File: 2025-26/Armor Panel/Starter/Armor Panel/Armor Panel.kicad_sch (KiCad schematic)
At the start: 10 parts

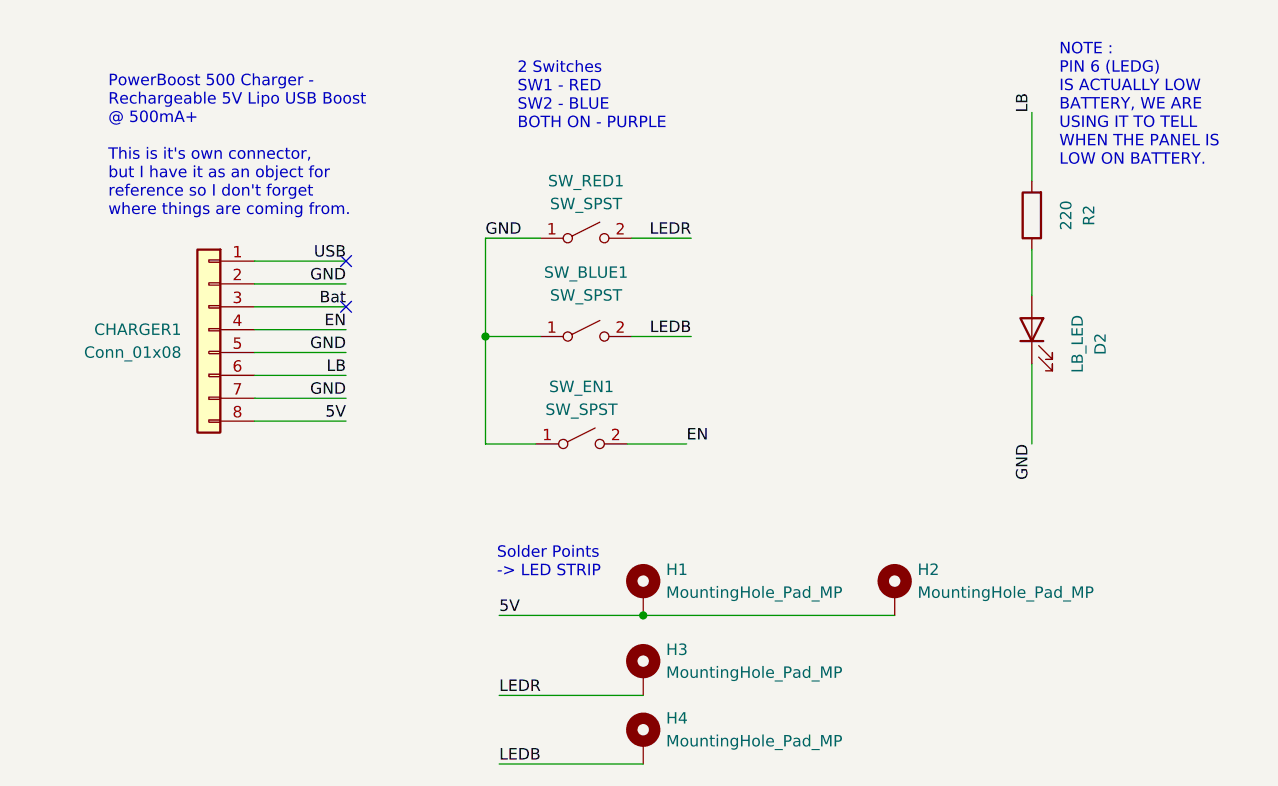
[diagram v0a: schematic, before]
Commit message: Forgot to connect pads
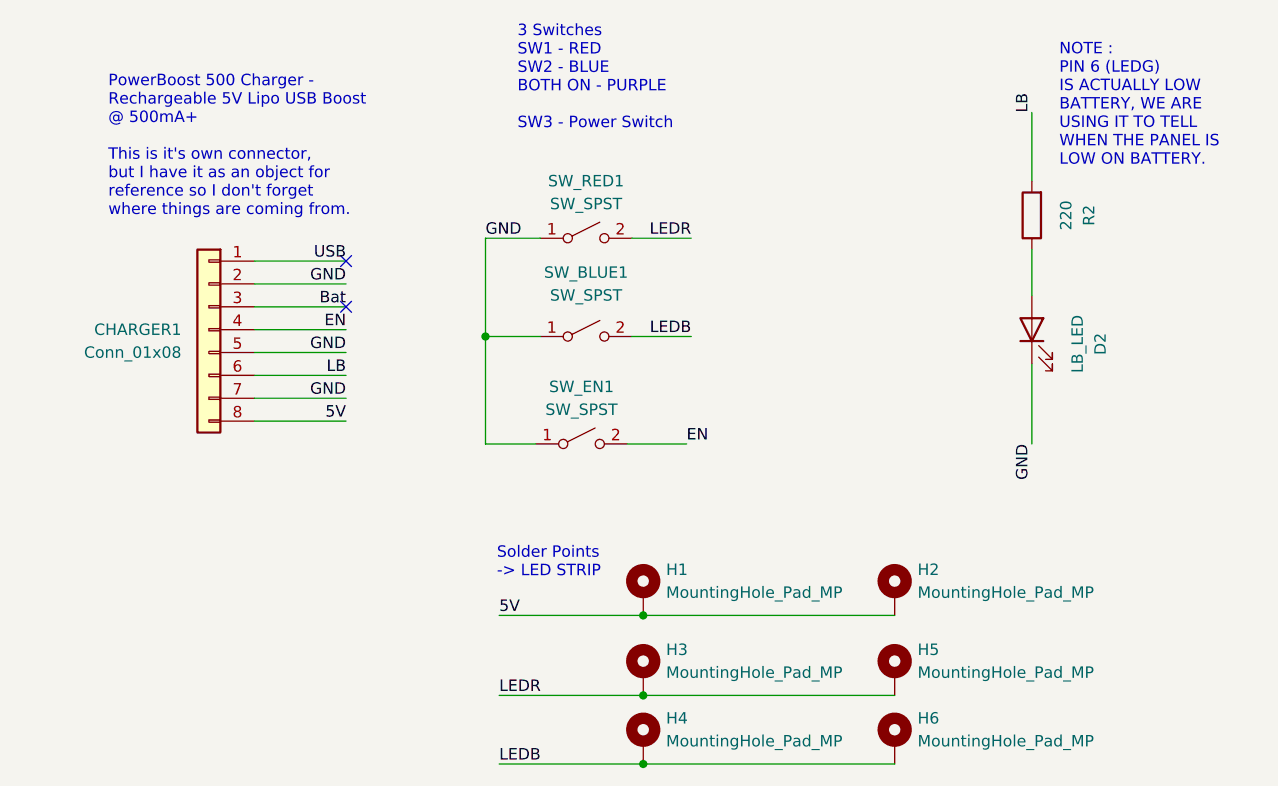
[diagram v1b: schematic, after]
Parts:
- added H5, H6: MountingHole_Pad_MP, symbol Mechanical:MountingHole_Pad_MP
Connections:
- net LEDB: now also H6.MP
- net LEDR: now also H5.MP
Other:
- note added: "3 Switches SW1 - RED SW2 - BLUE BOTH ON - PURPLE SW3 - Power Switch"
- note removed: "2 Switches SW1 - RED SW2 - BLUE BOTH ON - PURPLE"
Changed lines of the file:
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@@
 		)
 	)
-	(text "2 Switches \nSW1 - RED\nSW2 - BLUE\nBOTH ON - PURPLE"
+	(text "3 Switches \nSW1 - RED\nSW2 - BLUE\nBOTH ON - PURPLE\n\nSW3 - Power Switch"
 		(exclude_from_sim no)
 		(at 116.84 60.452 0)
@@
 			(justify left bottom)
 		)
+	)
+	(junction
+		(at 130.81 123.19)
+		(diameter 0)
+		(color 0 0 0 0)
+	)
+	(junction
+		(at 130.81 130.81)
+		(diameter 0)
+		(color 0 0 0 0)
 	)
 	(junction
@@
 	(wire
 		(pts
+			(xy 130.81 130.81) (xy 158.75 130.81)
+		)
+		(stroke
+			(width 0)
+			(type default)
+		)
+	)
+	(wire
+		(pts
 			(xy 113.284 72.39) (xy 119.38 72.39)
 		)
@@
 		(pts
 			(xy 135.636 95.25) (xy 129.032 95.25)
+		)
+		(stroke
+			(width 0)
+			(type default)
+		)
+	)
+	(wire
+		(pts
+			(xy 130.81 123.19) (xy 158.75 123.19)
 		)
 		(stroke
@@
 	(symbol
 		(lib_id "Mechanical:MountingHole_Pad_MP")
+		(at 158.75 128.27 0)
+		(unit 1)
+		(exclude_from_sim no)
+		(in_bom no)
+		(on_board yes)
+		(dnp no)
+		(fields_autoplaced yes)
+		(property "Reference" "H6"
+			(at 161.29 125.7299 0)
+			(effects
+				(font
+					(size 1.27 1.27)
+				)
+				(justify left)
+			)
+		)
+		(property "Value" "MountingHole_Pad_MP"
+			(at 161.29 128.2699 0)
+			(effects
+				(font
+					(size 1.27 1.27)
+				)
+				(justify left)
+			)
+		)
+		(property "Footprint" ""
+			(at 158.75 128.27 0)
+			(effects
+				(font
+					(size 1.27 1.27)
+				)
+				(hide yes)
+			)
+		)
+		(property "Datasheet" "~"
+			(at 158.75 128.27 0)
+			(effects
+				(font
+					(size 1.27 1.27)
+				)
+				(hide yes)
+			)
+		)
+		(property "Description" "Mounting Hole with connection as pad named MP"
+			(at 158.75 128.27 0)
+			(effects
+				(font
+					(size 1.27 1.27)
+				)
+				(hide yes)
+			)
+		)
+		(pin "MP"
+		)
+		(instances
+			(project "Armor Panel"
+				(path "/8daf21d7-2a01-47b9-ae43-0884e5e5c5e2"
+					(reference "H6")
+					(unit 1)
+				)
+			)
+		)
+	)
+	(symbol
+		(lib_id "Mechanical:MountingHole_Pad_MP")
 		(at 130.81 111.76 0)
 		(unit 1)
@@
 					(unit 1)
 				)
+			)
+		)
+	)
+	(symbol
+		(lib_id "Mechanical:MountingHole_Pad_MP")
+		(at 158.75 120.65 0)
+		(unit 1)
+		(exclude_from_sim no)
+		(in_bom no)
+		(on_board yes)
+		(dnp no)
+		(fields_autoplaced yes)
+		(property "Reference" "H5"
+			(at 161.29 118.1099 0)
+			(effects
+				(font
+					(size 1.27 1.27)
+				)
+				(justify left)
+			)
+		)
+		(property "Value" "MountingHole_Pad_MP"
+			(at 161.29 120.6499 0)
+			(effects
+				(font
+					(size 1.27 1.27)
+				)
+				(justify left)
+			)
+		)
+		(property "Footprint" ""
+			(at 158.75 120.65 0)
+			(effects
+				(font
+					(size 1.27 1.27)
+				)
+				(hide yes)
+			)
+		)
+		(property "Datasheet" "~"
+			(at 158.75 120.65 0)
+			(effects
+				(font
+					(size 1.27 1.27)
+				)
+				(hide yes)
+			)
+		)
+		(property "Description" "Mounting Hole with connection as pad named MP"
+			(at 158.75 120.65 0)
+			(effects
+				(font
+					(size 1.27 1.27)
+				)
+				(hide yes)
+			)
+		)
+		(pin "MP"
+		)
+		(instances
+			(project "Armor Panel"
+				(path "/8daf21d7-2a01-47b9-ae43-0884e5e5c5e2"
+					(reference "H5")
+					(unit 1)
+				)

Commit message: Added new switch for improved armor plating
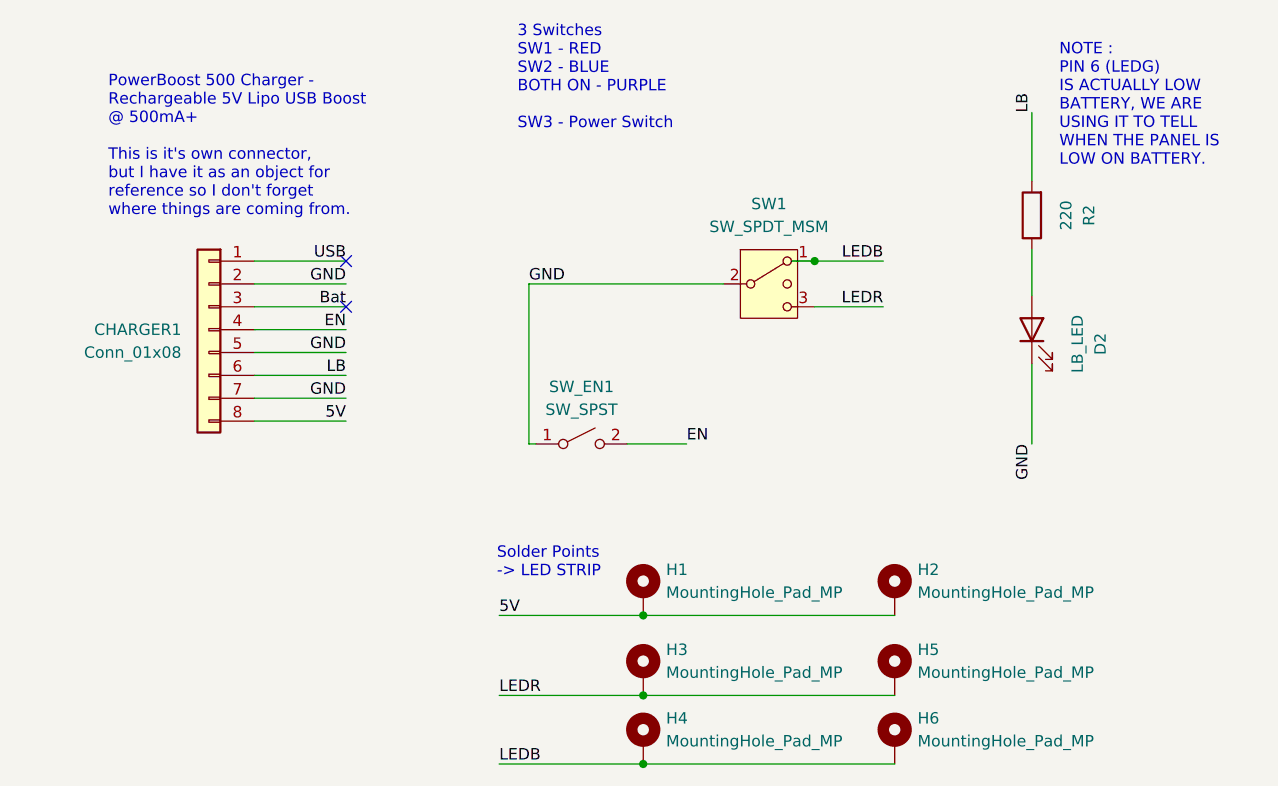
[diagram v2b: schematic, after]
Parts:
- removed SW_BLUE1, SW_RED1: SW_SPST, RB141C1100:SW_RB141C1100, symbol Switch:SW_SPST
- added SW1: SW_SPDT_MSM, symbol Switch:SW_SPDT_MSM
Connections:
- net GND: now also SW1.2 (3)
- net LEDB: now also SW1.1
- net LEDR: now also SW1.3 (4)
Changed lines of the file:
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@@
+	)
+	(junction
+		(at 149.86 74.93)
+		(diameter 0)
+		(color 0 0 0 0)
 	)
 	(junction
@@
 		(color 0 0 0 0)
 	)
-	(junction
-		(at 113.284 83.312)
-		(diameter 0)
-		(color 0 0 0 0)
-	)
 	(no_connect
 		(at 97.79 80.01)
@@
 	(wire
 		(pts
-			(xy 113.284 95.25) (xy 118.872 95.25)
+			(xy 118.11 95.25) (xy 118.872 95.25)
 		)
 		(stroke
@@
 	(wire
 		(pts
-			(xy 113.284 72.39) (xy 119.38 72.39)
+			(xy 147.32 74.93) (xy 149.86 74.93)
 		)
 		(stroke
@@
 	(wire
 		(pts
+			(xy 118.11 77.47) (xy 139.7 77.47)
+		)
+		(stroke
+			(width 0)
+			(type default)
+		)
+	)
+	(wire
+		(pts
 			(xy 97.79 87.63) (xy 87.63 87.63)
 		)
@@
 	(wire
 		(pts
+			(xy 149.86 74.93) (xy 157.48 74.93)
+		)
+		(stroke
+			(width 0)
+			(type default)
+		)
+	)
+	(wire
+		(pts
 			(xy 114.808 123.19) (xy 130.81 123.19)
 		)
@@
 	(wire
 		(pts
-			(xy 129.54 72.39) (xy 136.144 72.39)
-		)
-		(stroke
-			(width 0)
-			(type default)
-		)
-	)
-	(wire
-		(pts
 			(xy 135.636 95.25) (xy 129.032 95.25)
 		)
@@
 	(wire
 		(pts
-			(xy 129.54 83.312) (xy 136.144 83.312)
+			(xy 149.86 80.01) (xy 157.48 80.01)
 		)
 		(stroke
@@
 	(wire
 		(pts
-			(xy 113.284 83.312) (xy 119.38 83.312)
-		)
-		(stroke
-			(width 0)
-			(type default)
-		)
-	)
-	(wire
-		(pts
 			(xy 173.99 86.36) (xy 173.99 95.25)
 		)
@@
 	(wire
 		(pts
-			(xy 113.284 95.25) (xy 113.284 83.312)
-		)
-		(stroke
-			(width 0)
-			(type default)
-		)
-	)
-	(wire
-		(pts
-			(xy 113.284 72.39) (xy 113.284 83.312)
+			(xy 118.11 77.47) (xy 118.11 95.25)
 		)
 		(stroke
@@
 	)
 	(label "GND"
-		(at 113.284 72.39 0)
+		(at 118.11 77.47 0)
 		(effects
 			(font
@@
 	)
 	(label "LEDB"
-		(at 136.144 83.312 180)
+		(at 157.48 74.93 180)
 		(effects
 			(font
@@
 	)
 	(label "LEDR"
-		(at 136.144 72.39 180)
+		(at 157.48 80.01 180)
 		(effects
 			(font
@@
 				(path "/8daf21d7-2a01-47b9-ae43-0884e5e5c5e2"
 					(reference "H2")
-					(unit 1)
-				)
-			)
-		)
-	)
-	(symbol
-		(lib_id "Switch:SW_SPST")
-		(at 124.46 83.312 0)
-		(unit 1)
-		(exclude_from_sim no)
-		(in_bom yes)
-		(on_board yes)
-		(dnp no)
-		(fields_autoplaced yes)
-		(property "Reference" "SW_BLUE1"
-			(at 124.46 76.2 0)
-			(effects
-				(font
-					(size 1.27 1.27)
-				)
-			)
-		)
-		(property "Value" "SW_SPST"
-			(at 124.46 78.74 0)
-			(effects
-				(font
-					(size 1.27 1.27)
-				)
-			)
-		)
-		(property "Footprint" "RB141C1100:SW_RB141C1100"
-			(at 124.46 83.312 0)
-			(effects
-				(font
-					(size 1.27 1.27)
-				)
-				(hide yes)
-			)
-		)
-		(property "Datasheet" "~"
-			(at 124.46 83.312 0)
-			(effects
-				(font
-					(size 1.27 1.27)
-				)
-				(hide yes)
-			)
-		)
-		(property "Description" ""
-			(at 124.46 83.312 0)
-			(effects
-				(font
-					(size 1.27 1.27)
-				)
-				(hide yes)
-			)
-		)
-		(pin "1"
-		)
-		(pin "2"
-		)
-		(instances
-			(project "Armor Panel"
-				(path "/8daf21d7-2a01-47b9-ae43-0884e5e5c5e2"
-					(reference "SW_BLUE1")
 					(unit 1)
 				)
@@
 	)
 	(symbol
+		(lib_id "Switch:SW_SPDT_MSM")
+		(at 144.78 77.47 0)
+		(unit 1)
+		(exclude_from_sim no)
+		(in_bom yes)
+		(on_board yes)
+		(dnp no)
+		(fields_autoplaced yes)
+		(property "Reference" "SW1"
+			(at 144.78 68.58 0)
+			(effects
+				(font
+					(size 1.27 1.27)
+				)
+			)
+		)
+		(property "Value" "SW_SPDT_MSM"
+			(at 144.78 71.12 0)
+			(effects
+				(font
+					(size 1.27 1.27)
+				)
+			)
+		)
+		(property "Footprint" ""
+			(at 130.81 66.04 0)
+			(effects
+				(font
+					(size 1.27 1.27)
+				)
+				(hide yes)
+			)
+		)
+		(property "Datasheet" "~"
+			(at 144.78 85.09 0)
+			(effects
+				(font
+					(size 1.27 1.27)
+				)
+				(hide yes)
+			)
+		)
+		(property "Description" "Switch, single pole double throw, center OFF position"
+			(at 144.78 77.47 0)
+			(effects
+				(font
+					(size 1.27 1.27)
+				)
+				(hide yes)
+			)
+		)
+		(pin "1"
+		)
+		(pin "3"
+		)
+		(pin "2"
+		)
+		(instances
+			(project ""
+				(path "/8daf21d7-2a01-47b9-ae43-0884e5e5c5e2"
+					(reference "SW1")
+					(unit 1)
+				)
+			)
+		)
+	)
+	(symbol
 		(lib_id "Mechanical:MountingHole_Pad_MP")
 		(at 158.75 128.27 0)
@@
 					(unit 1)
 				)
-			)
-		)
-	)
-	(symbol
-		(lib_id "Switch:SW_SPST")
-		(at 124.46 72.39 0)
-		(unit 1)
-		(exclude_from_sim no)
-		(in_bom yes)
-		(on_board yes)
-		(dnp no)
-		(fields_autoplaced yes)
-		(property "Reference" "SW_RED1"
-			(at 124.46 66.04 0)
-			(effects
-				(font
-					(size 1.27 1.27)
-				)
-			)
-		)
-		(property "Value" "SW_SPST"
-			(at 124.46 68.58 0)
-			(effects
-				(font
-					(size 1.27 1.27)
-				)
-			)
-		)
-		(property "Footprint" "RB141C1100:SW_RB141C1100"
-			(at 124.46 72.39 0)
-			(effects
-				(font
-					(size 1.27 1.27)
-				)
-				(hide yes)
-			)
-		)
-		(property "Datasheet" "~"
-			(at 124.46 72.39 0)
-			(effects
-				(font
-					(size 1.27 1.27)
-				)
-				(hide yes)
-			)
-		)
-		(property "Description" ""
-			(at 124.46 72.39 0)
-			(effects
-				(font
-					(size 1.27 1.27)
-				)
-				(hide yes)
-			)
-		)
-		(pin "1"
-		)
-		(pin "2"
-		)
-		(instances
-			(project "Armor Panel"
-				(path "/8daf21d7-2a01-47b9-ae43-0884e5e5c5e2"
-					(reference "SW_RED1")
-					(unit 1)
-				)

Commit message: My Armor Panel
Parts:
- CHARGER1: footprint (none) -> Component Library:Power Boost Board
- H1, H2, H3, H4, H5, H6: footprint (none) -> Component Library:Wire THT Pad
- SW1: footprint (none) -> Component Library:SPDT
- SW_EN1: footprint RB141C1100:SW_RB141C1100 -> Component Library:SPST
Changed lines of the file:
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@@
 			)
 		)
-		(property "Footprint" ""
+		(property "Footprint" "Component Library:Wire THT Pad"
 			(at 130.81 120.65 0)
 			(effects
@@
 			)
 		)
-		(property "Footprint" ""
+		(property "Footprint" "Component Library:Wire THT Pad"
 			(at 158.75 111.76 0)
 			(effects
@@
 			)
 		)
-		(property "Footprint" "RB141C1100:SW_RB141C1100"
+		(property "Footprint" "Component Library:SPST"
 			(at 123.952 95.25 0)
 			(effects
@@
 			)
 		)
-		(property "Footprint" ""
+		(property "Footprint" "Component Library:Power Boost Board"
 			(at 82.55 82.55 0)
 			(effects
@@
 			)
 		)
-		(property "Footprint" ""
+		(property "Footprint" "Component Library:SPDT"
 			(at 130.81 66.04 0)
 			(effects
@@
 			)
 		)
-		(property "Footprint" ""
+		(property "Footprint" "Component Library:Wire THT Pad"
 			(at 158.75 128.27 0)
 			(effects
@@
 			)
 		)
-		(property "Footprint" ""
+		(property "Footprint" "Component Library:Wire THT Pad"
 			(at 130.81 111.76 0)
 			(effects
@@
 			)
 		)
-		(property "Footprint" ""
+		(property "Footprint" "Component Library:Wire THT Pad"
 			(at 158.75 120.65 0)
 			(effects
@@
 			)
 		)
-		(property "Footprint" ""
+		(property "Footprint" "Component Library:Wire THT Pad"
 			(at 130.81 128.27 0)
 			(effects

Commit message: Fixed Connectors
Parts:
- removed H1, H2, H3, H4, H5, H6: MountingHole_Pad_MP, Component Library:Wire THT Pad, symbol Mechanical:MountingHole_Pad_MP
- added J1, J2, J3, J4, J5, J6: Conn_01x01_Pin, Component Library:Wire THT Pad, symbol Connector:Conn_01x01_Pin
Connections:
- net 5V: now also J1.1 (Pin_1), J2.1 (Pin_1)
- net LEDB: now also J5.1 (Pin_1), J6.1 (Pin_1)
- net LEDR: now also J3.1 (Pin_1), J4.1 (Pin_1)

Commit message: Unholy Abomination
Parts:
- removed J1, J2, J3, J4, J5, J6: Conn_01x01_Pin, Component Library:Wire THT Pad, symbol Connector:Conn_01x01_Pin
- removed SW1: SW_SPDT_MSM, Component Library:SPDT, symbol Switch:SW_SPDT_MSM
- removed SW_EN1: SW_SPST, Component Library:SPST, symbol Switch:SW_SPST
- added J1, J2, J3: Conn_01x03, Connector_JST:JST_PH_B3B-PH-K_1x03_P2.00mm_Vertical, symbol Connector_Generic:Conn_01x03
- added J4, J5: Conn_01x02, Connector_JST:JST_PH_B2B-PH-K_1x02_P2.00mm_Vertical, symbol Connector_Generic:Conn_01x02
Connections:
- net 5V: now also J1.1 (Pin_1), J2.1 (Pin_1)
- net EN: now also J5.1 (Pin_1)
- net GND: now also J3.3 (Pin_3), J4.2 (Pin_2), J5.2 (Pin_2)
- net LEDB: now also J1.3 (Pin_3), J2.3 (Pin_3), J3.1 (Pin_1)
- net LEDR: now also J1.2 (Pin_2), J2.2 (Pin_2), J3.2 (Pin_2)
- net USB: now also J4.1 (Pin_1)
- no-connect marks 2 -> 1
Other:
- moved on the sheet: CHARGER1
